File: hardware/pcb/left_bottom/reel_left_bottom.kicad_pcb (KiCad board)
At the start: 2 copper layers, 145.9 x 95.9 mm, 8 parts, among them SW18 SW_Push, SW19 SW_Push, SW25 RotaryEncoder

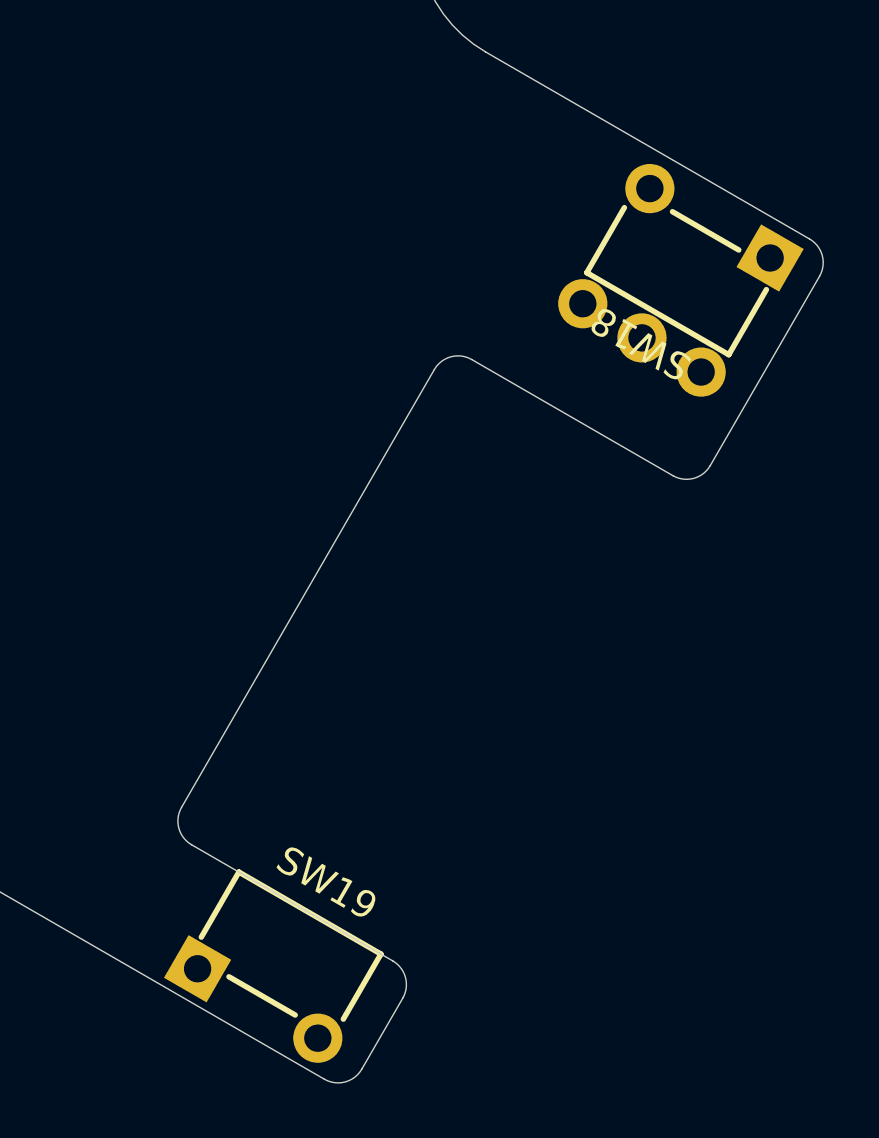
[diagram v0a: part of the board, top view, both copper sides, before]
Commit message: Update hardware assets and trackball profiler
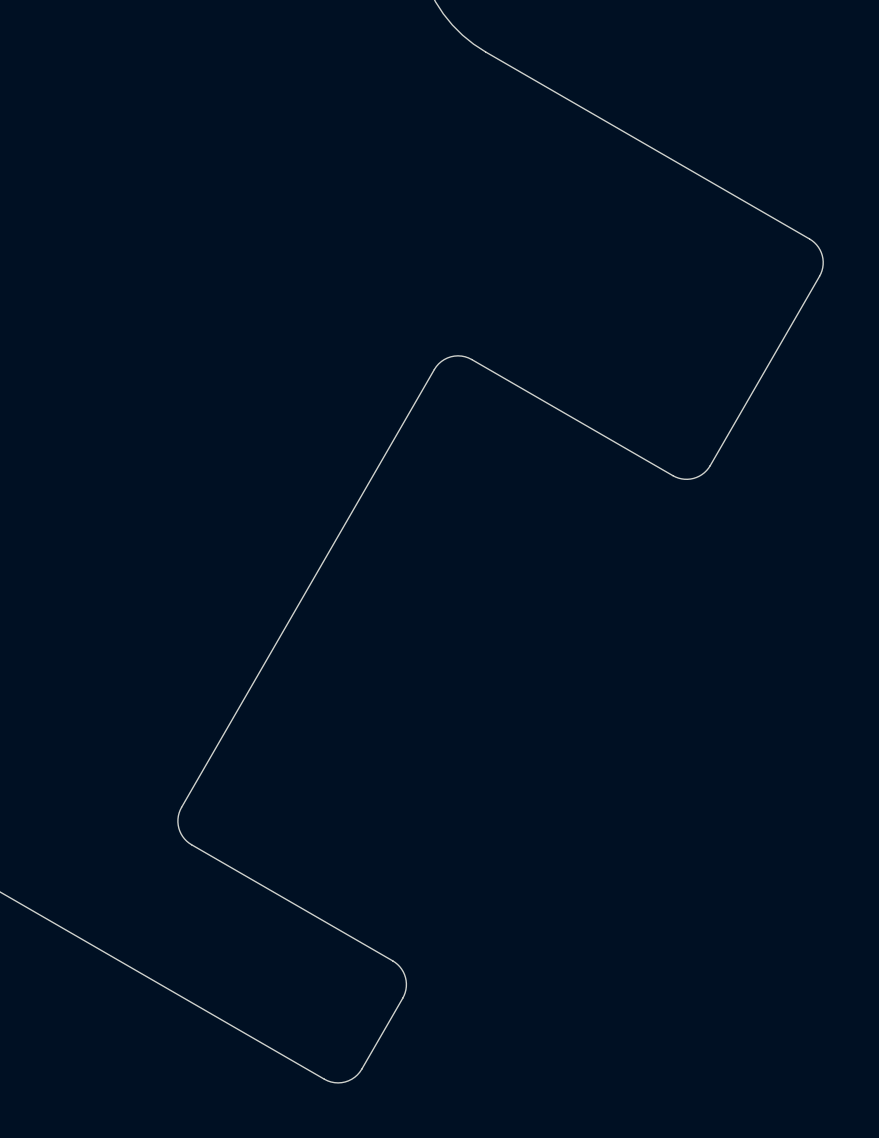
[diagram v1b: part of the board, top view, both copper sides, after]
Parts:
- removed SW18, SW19: SW_Push, reel:Switch_Tactile_6x6x3.5_Vertical_THT_5.08mm
- removed SW25: RotaryEncoder, reel:RotaryEncoder_BM10_3Pin

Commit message: Update ReeL PCB and mechanical assets
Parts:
- removed the Ref** at (169.5, 58.2)
- removed the Ref** at (142.5, 114.0)
- removed the Ref** at (189.5, 115.0)
- removed the Ref** at (94.0, 115.0)
- removed the Ref** at (112.0, 58.0)
- added Ref**: MountingHole_2.2mm_M2, MountingHole:MountingHole_2.2mm_M2, F.Cu at (112.5, 71.5)
- added Ref**: MountingHole_2.2mm_M2, MountingHole:MountingHole_2.2mm_M2, F.Cu at (169.0, 74.5)
- added Ref**: MountingHole_2.2mm_M2, MountingHole:MountingHole_2.2mm_M2, F.Cu at (140.5, 115.0)
- added Ref**: MountingHole_2.2mm_M2, MountingHole:MountingHole_2.2mm_M2, F.Cu at (93.5, 100.5)
- added Ref**: MountingHole_2.2mm_M2, MountingHole:MountingHole_2.2mm_M2, F.Cu at (189.5, 117.0)
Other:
- board size 145.9 x 95.9 mm -> 150.6 x 100.3 mm
